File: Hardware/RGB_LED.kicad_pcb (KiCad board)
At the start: 2 copper layers, 34.3 x 34.3 mm, 17 parts, among them IC1 ATTINY13A-SS, P1 CONN_01X06, Q1 MMBT3904, Q2 MMBT3904, Q3 MMBT3904, SW1 SW_PUSH, SW2 Switch_SPDT_x2

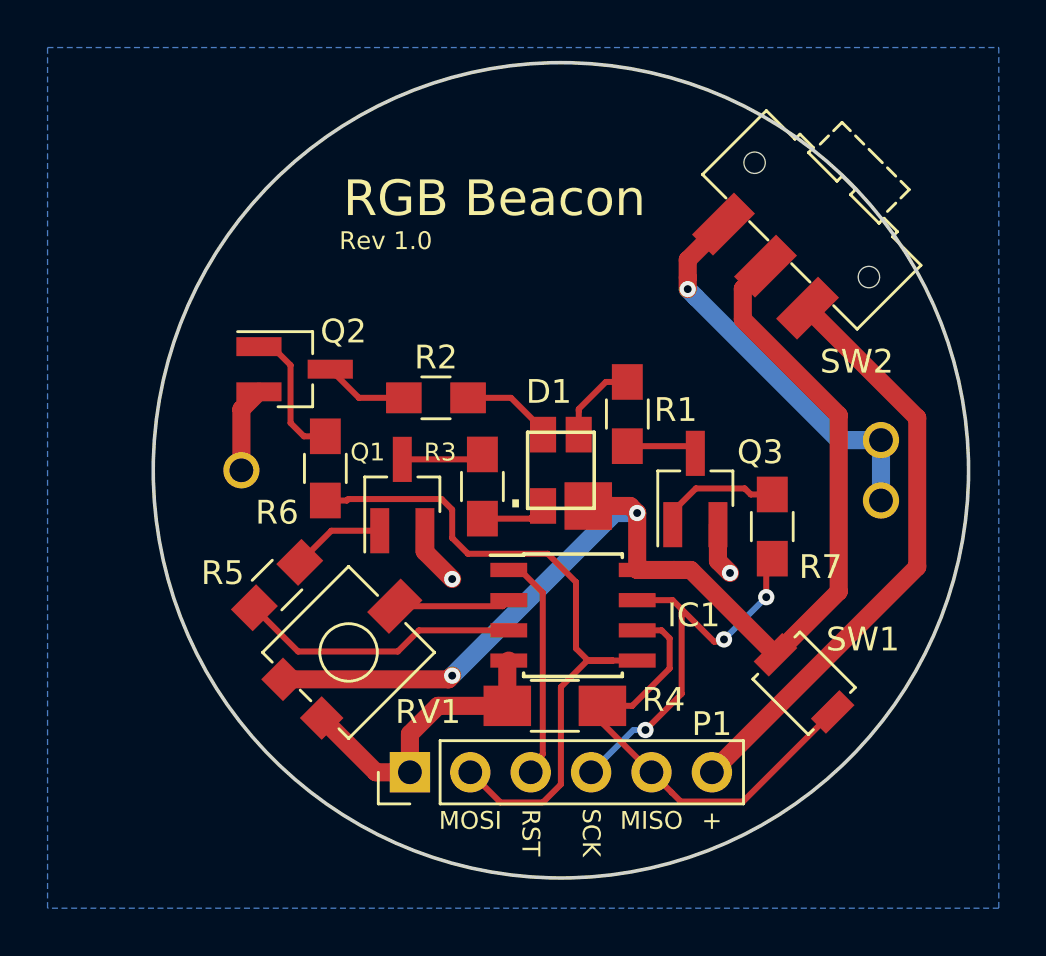
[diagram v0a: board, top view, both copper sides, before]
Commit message: Add decoupling cap
Fix #1
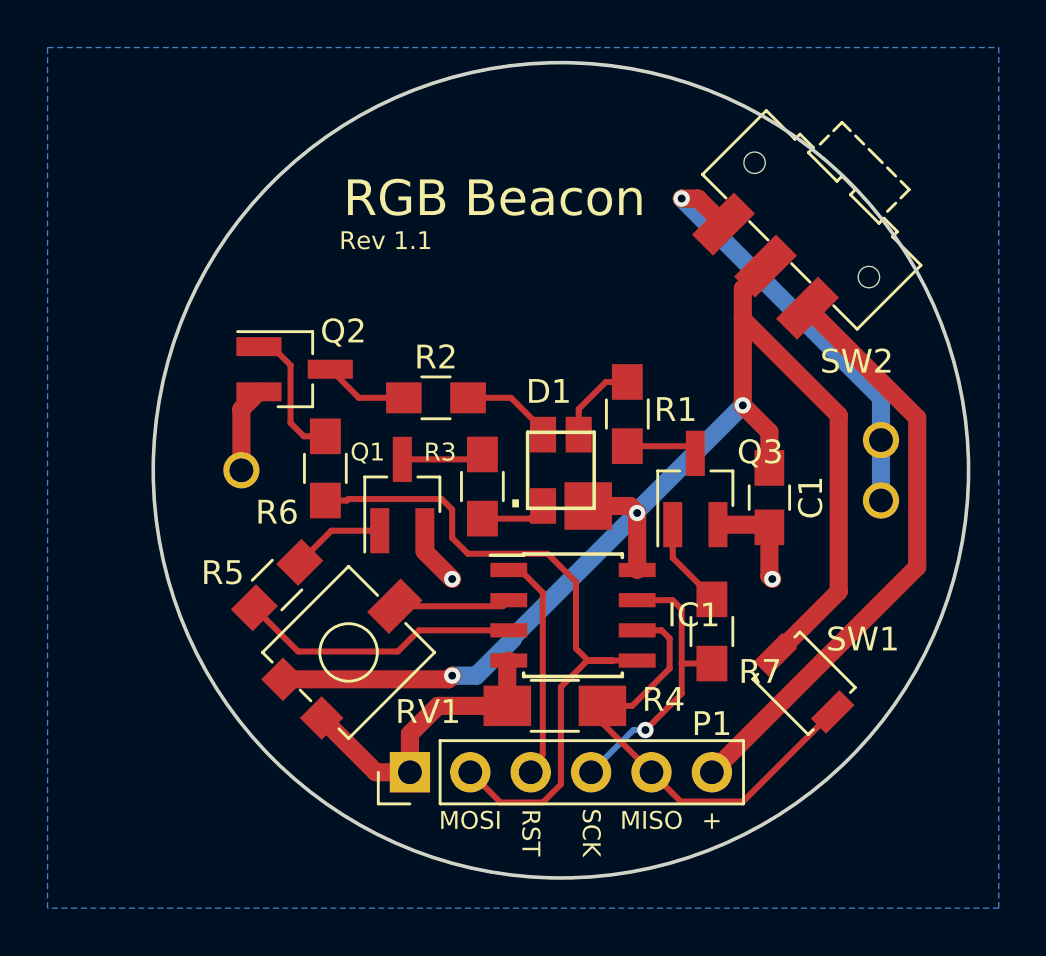
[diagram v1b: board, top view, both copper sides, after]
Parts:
- added C1: 0.1uF, Capacitors_SMD:C_0805_HandSoldering, F.Cu at (157.4, 82.4)
- R1: value 62 -> 8
- R2: value 56 -> 8
- R3: value 100 -> 36
- R5, R6, R7: value R -> 7k2
- moved R7 5.09 mm to (154.9, 88.1)
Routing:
- net +3V3: track 49.2 -> 55.0 mm, vias 2 -> 3
- net /Blue: track 18.1 -> 12.8 mm, vias 3 -> 1
- net GND: track 21.1 -> 23.3 mm
- net Net-(BT1-Pad1): track 16.7 -> 18.4 mm
- net Net-(Q3-Pad1): track 5.24 -> 4.37 mm
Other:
- board text added: "Rev 1.1"
- board text removed: "Rev 1.0"

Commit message: Board rev 1.2
+ Add 10k resistor to reset
+ Switch and trim moved to back for better ux
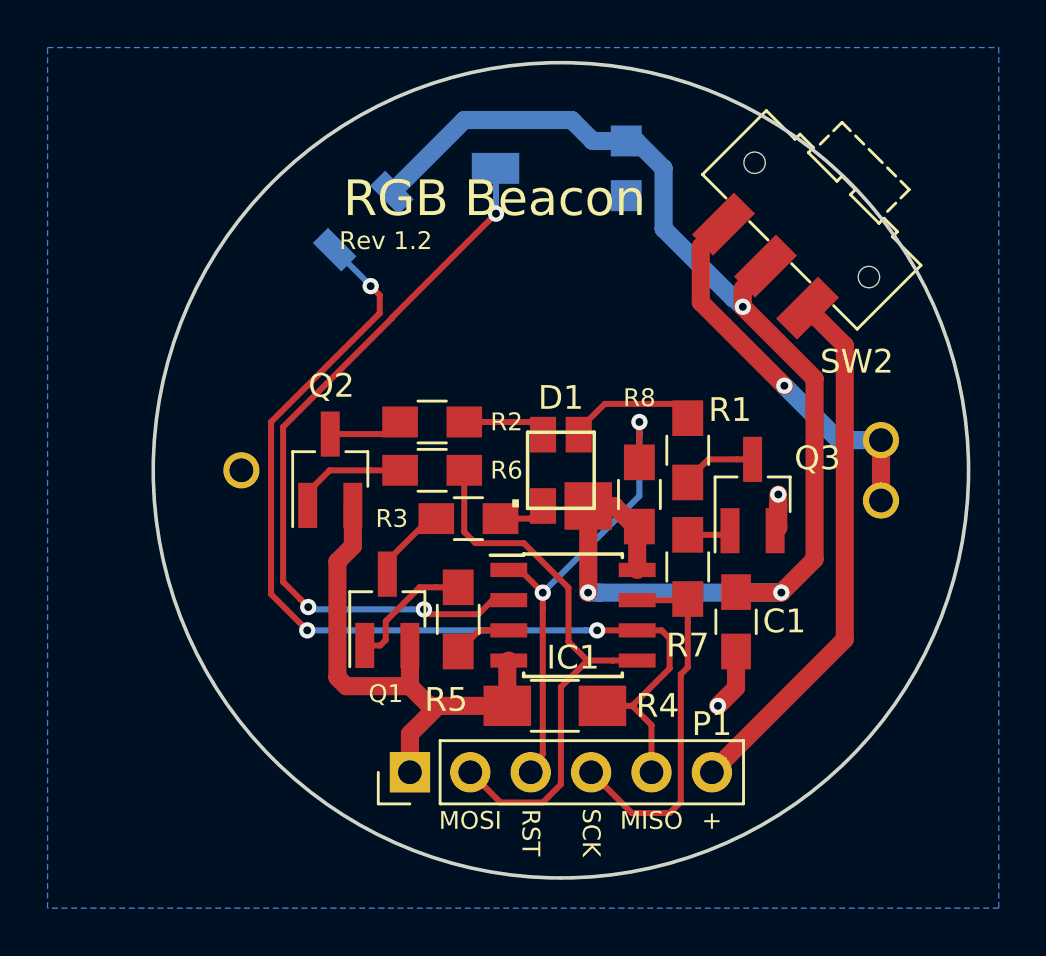
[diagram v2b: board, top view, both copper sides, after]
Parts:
- added R8: 10k, Resistors_SMD:R_0805_HandSoldering, F.Cu at (151.9, 82.3)
- RV1, SW1: moved to B.Cu
- moved SW1 26.9 mm to (140.3, 70.8), turned to 225 degrees
- moved RV1 22.2 mm to (148.6, 68.6), turned to 0 degrees
- moved R5 7.76 mm to (144.3, 87.5), turned to 90 degrees
- moved C1 5.41 mm to (156.0, 87.7)
- moved Q1 4.87 mm to (141.3, 87.1)
- moved R6 4.49 mm to (143.2, 81.3), turned to 180 degrees
- moved Q2 4.49 mm to (138.9, 81.3), turned to 90 degrees
- moved R1 2.96 mm to (153.9, 80.4)
- moved R7 2.90 mm to (153.9, 85.3)
- moved Q3 2.42 mm to (156.7, 82.3)
- moved R3 1.47 mm to (144.7, 83.3), turned to 0 degrees
- moved R2 1.03 mm to (143.2, 79.2)
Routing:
- net /Trim: track 4.90 -> 31.4 mm, vias 0 -> 3
- net /Switch: track 19.6 -> 43.3 mm, vias 0 -> 3
- net Net-(IC1-Pad1): track 9.59 -> 20.1 mm, vias 0 -> 2
- net /Red: track 11.8 -> 2.49 mm
- net /Green: track 30.1 -> 24.2 mm
- net /Blue: track 12.8 -> 16.2 mm, vias 1 -> 0
- net GND: track 23.3 -> 26.2 mm
- net /ICP_PWR: track 25.0 -> 22.5 mm
- net Net-(Q3-Pad1): track 4.37 -> 1.85 mm
- net Net-(BT1-Pad1): track 18.4 -> 16.2 mm
- net Net-(D1-Pad3): track 3.59 -> 5.55 mm
- net Net-(Q1-Pad1): track 3.91 -> 5.41 mm
- net Net-(Q2-Pad3): track 4.22 -> 3.15 mm
- net Net-(Q2-Pad1): track 5.88 -> 4.82 mm
- net Net-(D1-Pad1): track 3.10 -> 2.34 mm
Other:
- board text added: "Rev 1.2"
- board text removed: "Rev 1.1"
